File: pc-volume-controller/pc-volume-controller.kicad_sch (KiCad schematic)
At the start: 16 parts, among them U1 Arduino_Nano_v3.x

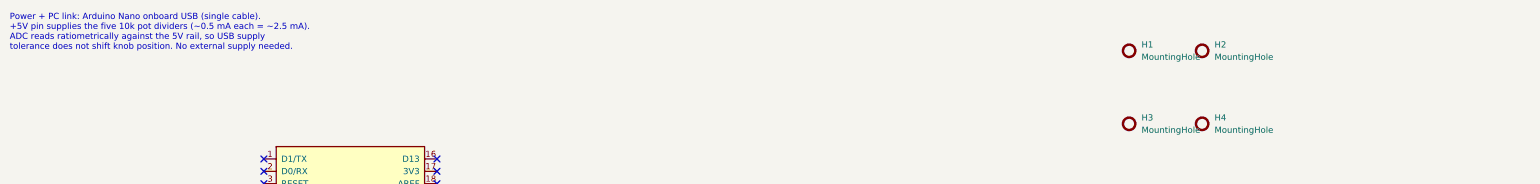
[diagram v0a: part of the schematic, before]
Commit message: Fix malformed s-expression: unescaped quotes broke KiCad's parser
KiCad refused to open the schematic:
    Error loading schematic ... line 919, offset 76. Expecting '('

Cause: the power-symbol Description properties embedded raw double
quotes inside a quoted string --
    (property "Description" "Power symbol creates a global label with name "+5V""
KiCad closes the string at 'name "', then hits a bare atom '+5V' followed
immediately by another quote and fails. Same fault at line 1030 (GND).

The kicad-happy sexp_parser accepted this, which is why the earlier
"PASS" verdict did not prove KiCad could load the file. Validation was
the weak link, not the design.

Fix
  - added esc() escaping (backslash then quote) to every string-emitting
    helper in both generators (property, label, text, pin name/number,
    fp_text, pad, net, footprint, gr_text)
  - de-quoted the two power-symbol Description strings

Validation added (strict, not lenient)
  - new strict s-expression checker enforcing: proper string escapes and
    termination, paren balance, single top-level list, '(' followed by an
    atom head, and lexical separation of adjacent value tokens
  - it reproduces KiCad's own diagnostic exactly: line 919 offset 76,
    ATOM('+5V') adjacent to STRING('')
  - both regenerated files pass; design re-verified unchanged:
    cross_verify 16/16 matched, 0 missing, 0 orphans, 0 value mismatches
    fab_release_gate 5 pass / 0 warn / 3 fail / 4 skip (unchanged)

Caveat unchanged: KiCad is not installed in this environment, so this fix
is validated by the strict checker and the skill's analyzer, not by KiCad
itself. Installing kicad-cli here would close that gap for good.
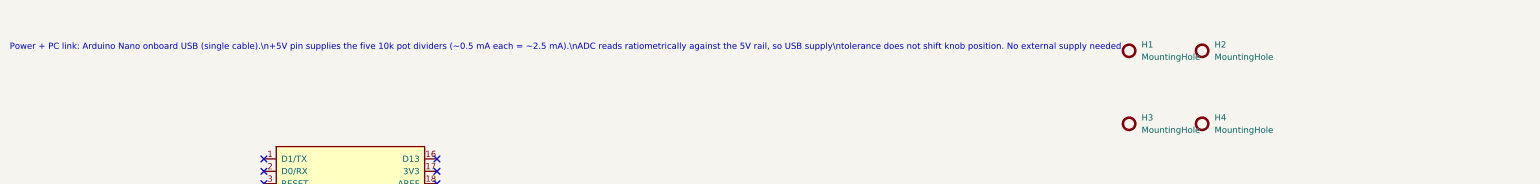
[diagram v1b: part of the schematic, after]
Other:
- note added: "Power + PC link: Arduino Nano onboard USB (single cable).\n+5V pin supplies the five 10k pot dividers (~0.5 mA each = ~2.5 mA).\nADC reads ratiometrically against the 5V rail, so USB supply\ntolerance does not shift knob position. No external supply needed."
- note removed: "Power + PC link: Arduino Nano onboard USB (single cable). +5V pin supplies the five 10k pot dividers (~0.5 mA each = ~2.5 mA). ADC reads ratiometrically against the 5V rail, so USB supply tolerance does not shift knob position. No external supply needed."
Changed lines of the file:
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@@
 		)
 	)
-	(text "Power + PC link: Arduino Nano onboard USB (single cable).\n+5V pin supplies the five 10k pot dividers (~0.5 mA each = ~2.5 mA).\nADC reads ratiometrically against the 5V rail, so USB supply\ntolerance does not shift knob position. No external supply needed."
+	(text "Power + PC link: Arduino Nano onboard USB (single cable).\\n+5V pin supplies the five 10k pot dividers (~0.5 mA each = ~2.5 mA).\\nADC reads ratiometrically against the 5V rail, so USB supply\\ntolerance does not shift knob position. No external supply needed."
 		(exclude_from_sim no)
 		(at 40.0 60.0 0)

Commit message: Fix double-escaped newline in the schematic design note
The esc() helper added in 5ab9944 escaped backslashes before converting
newlines, so the multi-line design note became a literal \\n (KiCad would
render a backslash and an n instead of line breaks). Cosmetic only -- the
file parsed fine either way -- but the note is there to be read.

esc() now escapes backslash, then quote, then turns a real newline into
KiCad's two-character \n escape; the note carries real newlines.

Strict checker passes; design unchanged (cross_verify 16/16 matched).
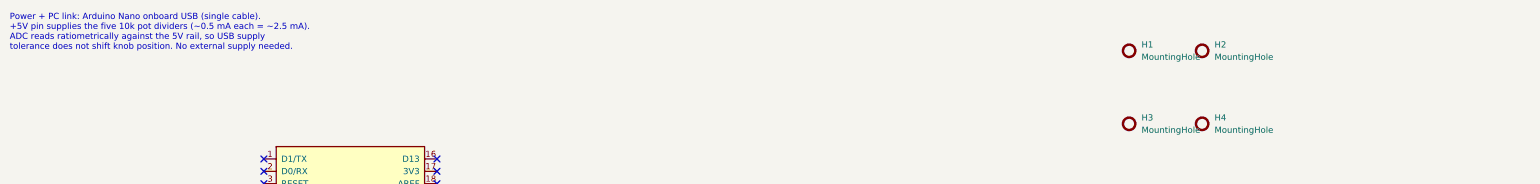
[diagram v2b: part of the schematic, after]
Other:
- note added: "Power + PC link: Arduino Nano onboard USB (single cable). +5V pin supplies the five 10k pot dividers (~0.5 mA each = ~2.5 mA). ADC reads ratiometrically against the 5V rail, so USB supply tolerance does not shift knob position. No external supply needed."
- note removed: "Power + PC link: Arduino Nano onboard USB (single cable).\n+5V pin supplies the five 10k pot dividers (~0.5 mA each = ~2.5 mA).\nADC reads ratiometrically against the 5V rail, so USB supply\ntolerance does not shift knob position. No external supply needed."
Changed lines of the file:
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@@
 		)
 	)
-	(text "Power + PC link: Arduino Nano onboard USB (single cable).\\n+5V pin supplies the five 10k pot dividers (~0.5 mA each = ~2.5 mA).\\nADC reads ratiometrically against the 5V rail, so USB supply\\ntolerance does not shift knob position. No external supply needed."
+	(text "Power + PC link: Arduino Nano onboard USB (single cable).\n+5V pin supplies the five 10k pot dividers (~0.5 mA each = ~2.5 mA).\nADC reads ratiometrically against the 5V rail, so USB supply\ntolerance does not shift knob position. No external supply needed."
 		(exclude_from_sim no)
 		(at 40.0 60.0 0)

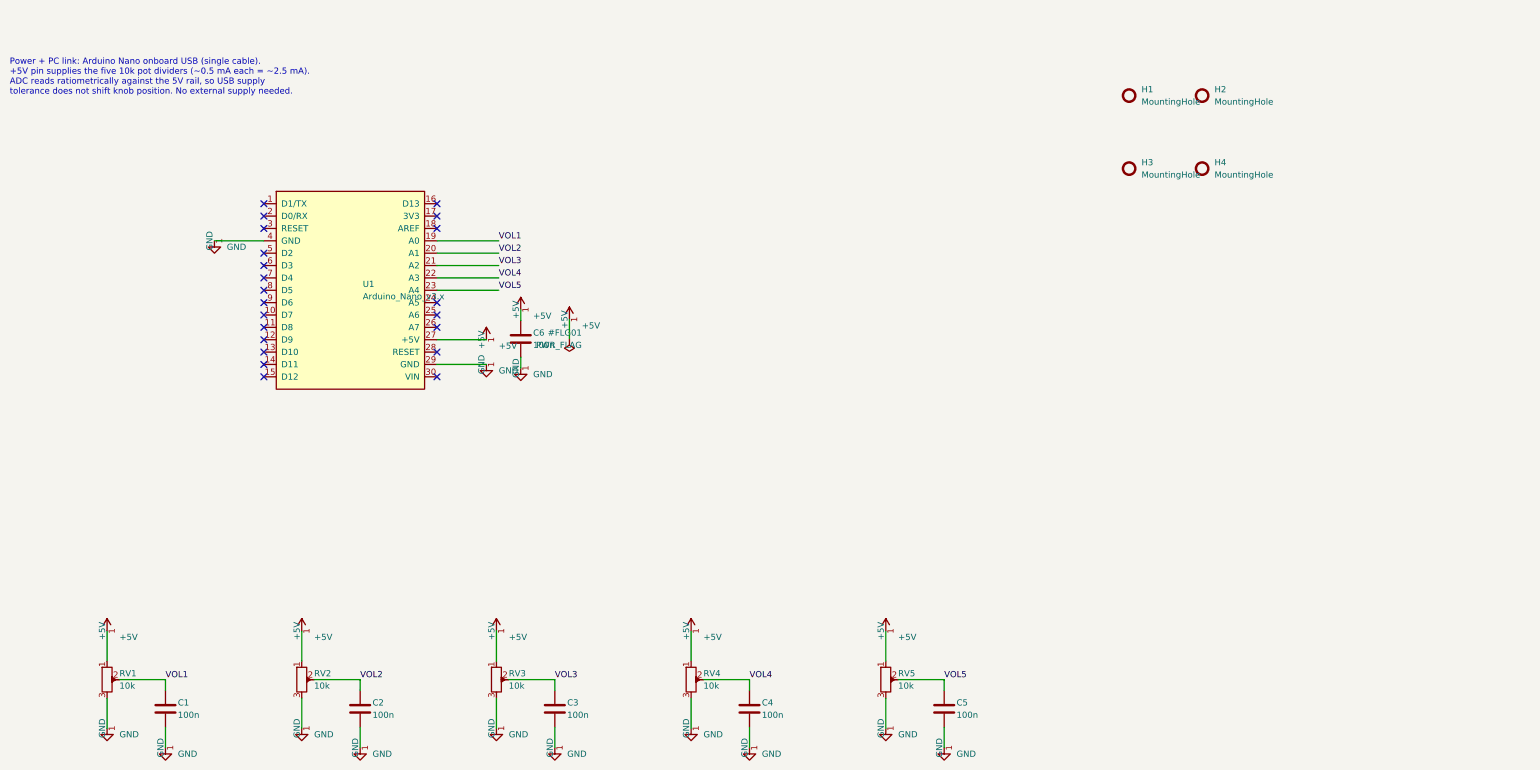
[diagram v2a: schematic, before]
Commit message: Rebuild with real KiCad 9 libraries; verified by kicad-cli ERC/DRC
KiCad is now installed on this host, so the generated project was validated
against KiCad itself rather than only the kicad-happy Python tooling. That
validation found real defects in what had been delivered:

pc-volume-controller.kicad_sch
* now embeds the actual MCU_Module:Arduino_Nano_v3.x, Device:R_Potentiometer,
  Device:C, power:* and Mechanical:MountingHole definitions instead of
  hand-authored symbols (fixes 37 lib_symbol_mismatch warnings)
* every coordinate snapped to the 1.27 mm grid (fixes 70 endpoint_off_grid)
* real library footprints assigned, replacing the invented 'pvc:' namespace
* ERC: 125 violations -> 0

The Nano pinout is now verified rather than assumed: the official symbol
confirms A0-A4 = pins 19-23, +5V = pin 27, GND = pins 4 and 29.

pc-volume-controller.kicad_pcb
* rebuilt from the real Module:Arduino_Nano, Potentiometer_THT and
  Capacitor_SMD footprints with all pads netted
* board fully routed on 2 layers (B.Cu horizontals, F.Cu verticals)
* DRC: 89 violations -> 0, with 0 unconnected items and 0 schematic-parity
  differences

LED/LED-revised.kicad_sch
* added the PWR_FLAG the GND net needs (the battery's negative pin is passive,
  so ERC reported power_pin_not_driven)
* ERC: 1 error -> 0

Validation notes: kicad-cli 9.0.2. Notable format findings - a .kicad_pcb may
not carry a top-level (uuid ...) node (KiCad refuses the board), gr_line stroke
type must be the bare atom 'solid' not a quoted string, and an embedded symbol
must keep leading atoms on its opening line.
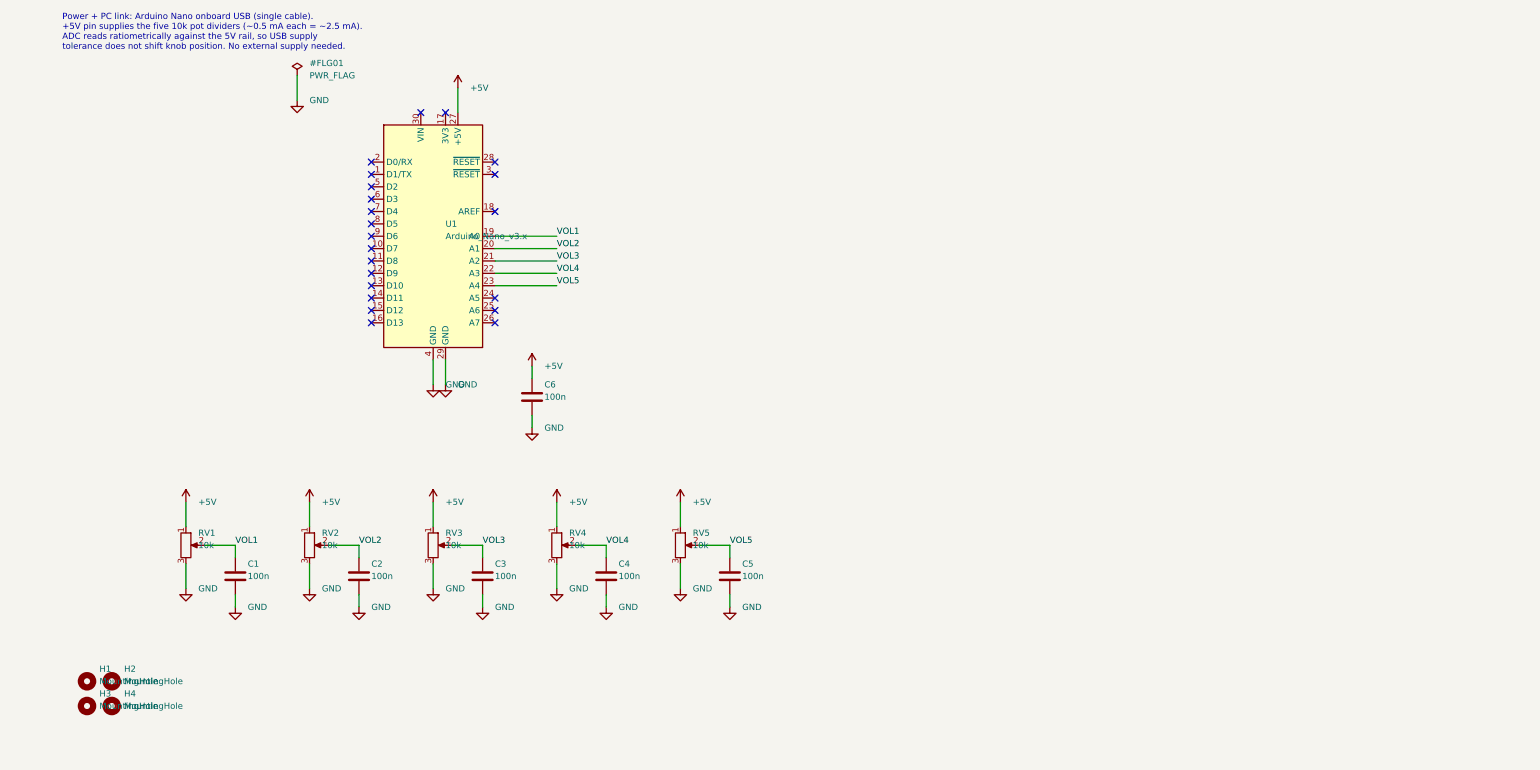
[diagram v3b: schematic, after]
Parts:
- removed U1: Arduino_Nano_v3.x, pvc:Arduino_Nano_30pin_THT, symbol Module:Arduino_Nano_v3.x
- added U1: Arduino_Nano_v3.x, Module:Arduino_Nano, symbol MCU_Module:Arduino_Nano_v3.x
- C1, C2, C3, C4, C5, C6: footprint pvc:C_0805_2012Metric -> Capacitor_SMD:C_0805_2012Metric
- H1, H2, H3, H4: footprint pvc:MountingHole_M3 -> MountingHole:MountingHole_3.2mm_M3
- RV1, RV2, RV3, RV4, RV5: footprint pvc:Potentiometer_9mm_PanelMount_THT -> Potentiometer_THT:Potentiometer_Alpha_RD901F-40-00D_Single_Vertical
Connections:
- net +5V: now also U1.27 (+5V)
- net GND: now also U1.29 (GND), U1.4 (GND)
- net VOL1: now also U1.19 (A0)
- net VOL2: now also U1.20 (A1)
- net VOL3: now also U1.21 (A2)
- net VOL4: now also U1.22 (A3)
- net VOL5: now also U1.23 (A4)
